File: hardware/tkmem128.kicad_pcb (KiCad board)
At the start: 2 copper layers, 78.7 x 66 mm, 24 parts, among them J1 Para a expansora, U1 GAL20V8B, U2 74HCT273, U3 AS6C1008-55PCN, U4 27C256

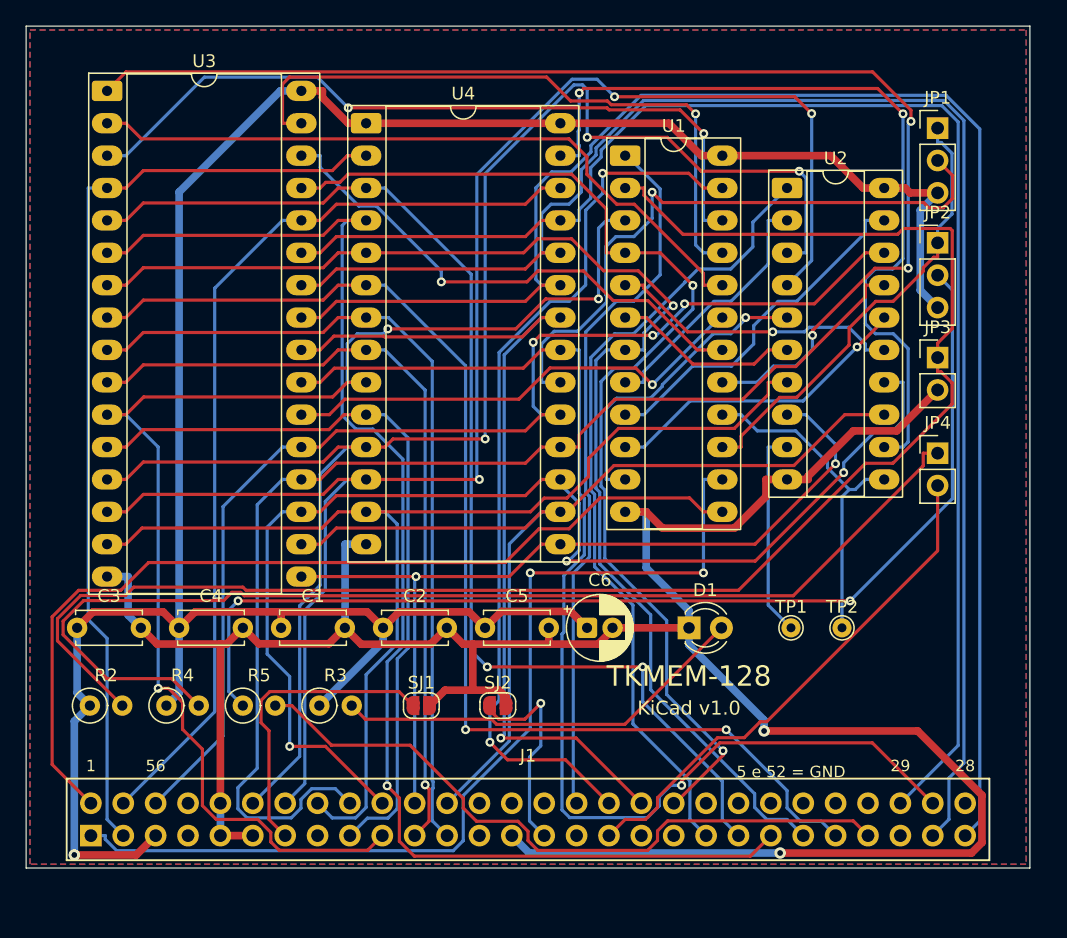
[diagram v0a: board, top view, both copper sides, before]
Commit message: Correcoes de revisao: pino 17, expansora dimensionada, .jed verificado
Correcoes apontadas na revisao:

- "Edu Luccas" -> "Eduardo Luccas" em toda a documentacao.

- O pino 17 do barramento NAO e livre no ZX Spectrum: os pinos 16, 17 e 18
  la sao Y, V e U do video componente. Corrigido na definicao do barramento
  e na documentacao, com aviso explicito de nunca fechar JP4 em Spectrum.
  Isso tambem sustenta a analise de por que a placa original avisava que o
  jumper na posicao errada danificava o micro: o pino util no TK e sinal de
  video no Spectrum, entao o jumper escolhia entre dois pinos diferentes, e
  os dois barramentos divergem justamente em pinos de alimentacao (34, 35,
  37).

- SJ1 e SJ2 sao opcionais e podem ficar abertos em qualquer maquina. O terra
  ja chega pelos pinos 6 e 14, que sao GND nas duas. Deixado explicito no
  README, na montagem e no verso da placa.

- Encaixe na caixa conferido contra os desenhos tecnicos da Patola: a tampa
  tem 81 x 69 mm internos e a placa principal (78,74 x 66,04) cabe com folga.
  Ja a expansora de 45 mm sobrava so 6,5 mm de cada lado da caixa de 32 mm -
  insuficiente para o soquete alcancar o TK. Alongada para 70 mm (19 mm de
  cada lado) e com as paredes da caixa marcadas na serigrafia.

- O .jed do GAL agora vai pronto: hardware/gal/tkmem128.jed, checksum C5752.
  Gerado por tools/galgen.py a partir das equacoes do projeto, com o mapa de
  colunas da matriz AND deduzido das proprias equacoes, e conferido fusivel a
  fusivel contra o mapa de referencia: zero divergencias em 2706 fusiveis.

Roteamento: as duas placas fecham 100% em 2 camadas com isolacao de 0,14 mm.
A ultima ligacao da placa principal exigiu um roteador de labirinto proprio
(tools/maze.py). ERC e DRC zerados; netlist reconferida no a no.

Co-Authored-By: Claude Opus 5 <noreply@anthropic.com>
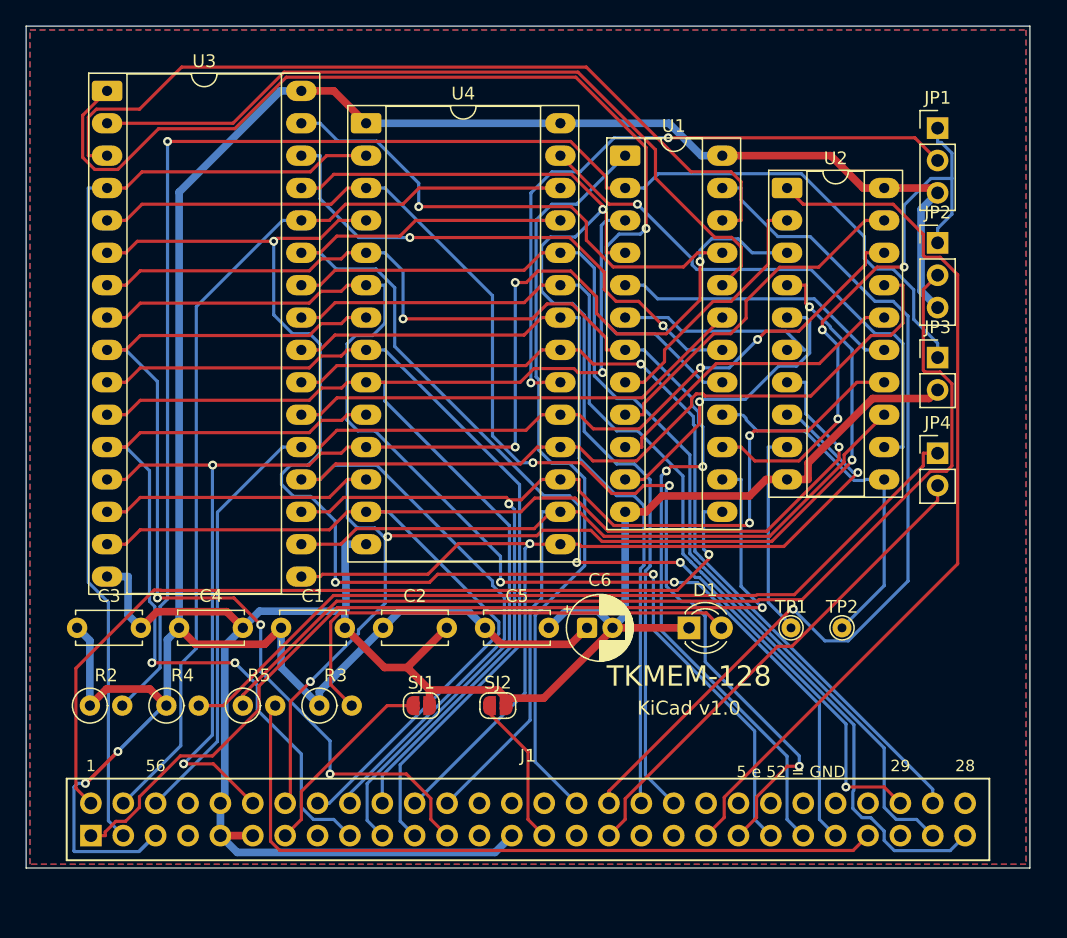
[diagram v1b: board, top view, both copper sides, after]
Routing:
- net GND: track 205.3 -> 157.9 mm, vias 2 -> 0
- net A11: track 125.8 -> 84.8 mm
- net A9: track 121.8 -> 81.7 mm
- net RAMDIS_DRV: track 88.9 -> 66.6 mm
- net A10: track 94.2 -> 72.1 mm
- net ROMA14: track 64.8 -> 42.8 mm, vias 2 -> 1
- net A8: track 114.4 -> 94.8 mm, vias 0 -> 3
- net D1: track 127.9 -> 109.8 mm, vias 3 -> 4
- net D0: track 124.9 -> 107.3 mm, vias 3 -> 5
- net D2: track 90.7 -> 105.5 mm, vias 0 -> 1
- net SA18: track 96.6 -> 83.0 mm, vias 3 -> 1
- net A3: track 65.7 -> 78.4 mm, vias 0 -> 3
- net ROMCS_N: track 35.7 -> 46.9 mm, vias 0 -> 3
- net ZX512: track 128.8 -> 117.6 mm, vias 0 -> 1
- net SA15: track 51.0 -> 40.1 mm
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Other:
- board text added: "NAO feche JP4 em ZX Spectrum: o pino 17 la e o V do video"
- board text added: "SJ1 e SJ2 sao terra extra, opcionais - podem ficar abertos"

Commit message: Esquematicos e silk rearranjados; pendencia do plano do soquete de borda
Esquematico das duas placas redesenhado a mao (havia simbolos saindo da
folha e sinais misturados) e serigrafia reorganizada. Conferido: ERC 0,
DRC 0, e a netlist exportada bate no a no com a intencao de projeto nas
duas placas (74 e 53 nets, zero divergencia).

Os geradores em tools/ passam a ser ferramenta de bootstrap: gen_schematic.py
e gen_pcb.py sobrescreveriam o ajuste manual. A fonte corrente e o conteudo
de hardware/. Documentado no README de tools/.

Registrada uma pendencia real da placa expansora (item 1b de
docs/ANTES-DE-FABRICAR.md): nas placas originais a fenda do soquete que
recebe os dedos do TK fica NO PLANO da placa, alinhada com os dedos de
passagem. O footprint atual e uma grade 2x28 de furos comuns, ou seja, o
conector monta por cima e a fenda fica alguns milimetros acima do plano —
o que joga a expansora abaixo do plano do TK e faz o periferico seguinte da
corrente descer outro tanto. Falta medir o conector para decidir entre
straddle mount e montagem por baixo.

Saidas de fabricacao e renders regerados a partir dos arquivos revisados.

Co-Authored-By: Claude Opus 5 <noreply@anthropic.com>
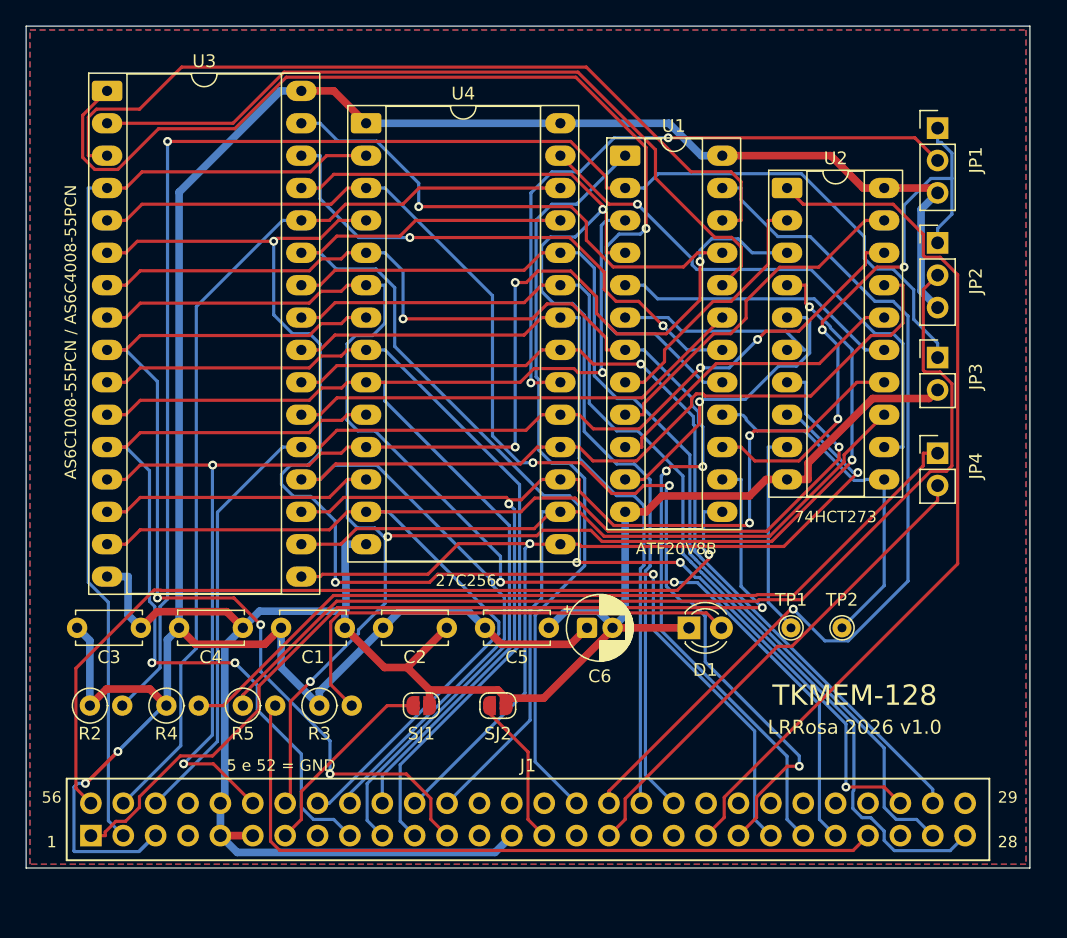
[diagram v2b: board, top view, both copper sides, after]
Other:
- board text added: "27C256"
- board text added: "74HCT273"
- board text added: "AS6C1008-55PCN / AS6C4008-55PCN"
- board text added: "ATF20V8B"
- board text added: "Derivado de Velesoft 2009 e Luccas Eletrônica 2012"
- board text added: "LRRosa 2026 v1.0"
- board text added: "NÃO feche JP4 em ZX Spectrum: o pino 17 lá é o V do vídeo"
- board text added: "SJ1 e SJ2 são terra extra, opcionais - podem ficar abertos"
- board text added: "SJ1 fechar SÓ em ZX Spectrum (pino 7 = GND lá)"
- board text added: "SJ2 fechar SÓ em TK90X/TK95 (pino 15 = GND lá)"
- board text removed: "Derivado de Velesoft 2009 e Luccas Eletronica 2012"
- board text removed: "KiCad v1.0"
- board text removed: "NAO feche JP4 em ZX Spectrum: o pino 17 la e o V do video"
- board text removed: "SJ1 e SJ2 sao terra extra, opcionais - podem ficar abertos"
- board text removed: "SJ1 fechar SO em ZX Spectrum (pino 7 = GND la)"
- board text removed: "SJ2 fechar SO em TK90X/TK95 (pino 15 = GND la)"
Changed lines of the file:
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@@
 		(tags "Through hole pin header THT 1x03 2.54mm single row")
 		(property "Reference" "JP2"
-			(at 0 -2.38 0)
+			(at 3 3 -90)
 			(layer "F.SilkS")
 			(effects
@@
 		(tags "test point THT pad")
 		(property "Reference" "TP2"
-			(at 0 -1.648 0)
+			(at 0 -2.2 0)
 			(layer "F.SilkS")
 			(effects
@@
 		(tags "Through hole pin header THT 1x03 2.54mm single row")
 		(property "Reference" "JP1"
-			(at 0 -2.38 0)
+			(at 3 2.5 -90)
 			(layer "F.SilkS")
 			(effects
@@
 		(tags "C Disc series Radial pin pitch 5.00mm diameter 5mm width 2.5mm Capacitor")
 		(property "Reference" "C5"
-			(at 2.5 -2.5 0)
+			(at 2.5 2.3 0)
 			(layer "F.SilkS")
 			(effects
@@
 		(tags "C Disc series Radial pin pitch 5.00mm diameter 5mm width 2.5mm Capacitor")
 		(property "Reference" "C4"
-			(at 2.5 -2.5 0)
+			(at 2.5 2.3 0)
 			(layer "F.SilkS")
 			(effects
@@
 		(tags "Resistor Axial_DIN0207 series Axial Vertical pin pitch 2.54mm 0.25W = 1/4W length 6.3mm diameter 2.5mm")
 		(property "Reference" "R3"
-			(at 1.27 -2.37 0)
+			(at 0 2.2 0)
 			(layer "F.SilkS")
 			(effects
@@
 		(tags "test point THT pad")
 		(property "Reference" "TP1"
-			(at 0 -1.648 0)
+			(at 0 -2.2 0)
 			(layer "F.SilkS")
 			(effects
@@
 		(tags "C Disc series Radial pin pitch 5.00mm diameter 5mm width 2.5mm Capacitor")
 		(property "Reference" "C2"
-			(at 2.5 -2.5 0)
+			(at 2.5 2.3 0)
 			(layer "F.SilkS")
 			(effects
@@
 		(tags "Through hole pin header THT 1x02 2.54mm single row")
 		(property "Reference" "JP4"
-			(at 0 -2.38 0)
+			(at 3 1 -90)
 			(layer "F.SilkS")
 			(effects
@@
 		(tags "Resistor Axial_DIN0207 series Axial Vertical pin pitch 2.54mm 0.25W = 1/4W length 6.3mm diameter 2.5mm")
 		(property "Reference" "R5"
-			(at 1.27 -2.37 0)
+			(at 0 2.2 0)
 			(layer "F.SilkS")
 			(effects
@@
 		(tags "header 2x28 TK90X TK95 interligacao placas")
 		(property "Reference" "J1"
-			(at 0 -5 0)
+			(at 0 -4.23 0)
 			(layer "F.SilkS")
 			(effects
@@
 			(layer "F.CrtYd")
 		)
-		(fp_text user "1"
-			(at -34.29 -4.2 0)
+		(fp_text user "56"
+			(at -37.37 -1.73 0)
 			(layer "F.SilkS")
 			(effects
@@
 			)
 		)
-		(fp_text user "56"
-			(at -29.21 -4.2 0)
+		(fp_text user "1"
+			(at -37.37 1.77 0)
 			(layer "F.SilkS")
 			(effects
@@
 		)
 		(fp_text user "29"
-			(at 29.21 -4.2 0)
+			(at 37.63 -1.73 0)
 			(layer "F.SilkS")
 			(effects
@@
 		)
 		(fp_text user "28"
-			(at 34.29 -4.2 0)
+			(at 37.63 1.77 0)
 			(layer "F.SilkS")
 			(effects
@@
 		(tags "CP Radial series Radial pin pitch 2.00mm diameter 5mm height 7mm Electrolytic Capacitor")
 		(property "Reference" "C6"
-			(at 1 -3.75 0)
+			(at 1 3.8 0)
 			(layer "F.SilkS")
 			(effects
@@
 		(tags "LED")
 		(property "Reference" "D1"
-			(at 1.27 -2.96 0)
+			(at 1.27 3.3 0)
 			(layer "F.SilkS")
 			(effects
@@
 		(tags "solder jumper open")
 		(property "Reference" "SJ1"
-			(at 0 -1.8 0)
+			(at 0 2.2 0)
 			(layer "F.SilkS")
 			(effects
@@
 		(tags "C Disc series Radial pin pitch 5.00mm diameter 5mm width 2.5mm Capacitor")
 		(property "Reference" "C1"
-			(at 2.5 -2.5 0)
+			(at 2.5 2.3 0)
 			(layer "F.SilkS")
 			(effects
@@
 		(tags "C Disc series Radial pin pitch 5.00mm diameter 5mm width 2.5mm Capacitor")
 		(property "Reference" "C3"
-			(at 2.5 -2.5 0)
+			(at 2.5 2.3 0)
 			(layer "F.SilkS")
 			(effects
@@
 		(tags "Resistor Axial_DIN0207 series Axial Vertical pin pitch 2.54mm 0.25W = 1/4W length 6.3mm diameter 2.5mm")
 		(property "Reference" "R4"
-			(at 1.27 -2.37 0)
+			(at 0 2.2 0)
 			(layer "F.SilkS")
 			(effects
@@
 		(tags "solder jumper open")
 		(property "Reference" "SJ2"
-			(at 0 -1.8 0)
+			(at 0 2.2 0)
 			(layer "F.SilkS")
 			(effects
@@
 		(tags "Resistor Axial_DIN0207 series Axial Vertical pin pitch 2.54mm 0.25W = 1/4W length 6.3mm diameter 2.5mm")
 		(property "Reference" "R2"
-			(at 1.27 -2.37 0)
+			(at 0 2.2 0)
 			(layer "F.SilkS")
 			(effects
@@
 		(tags "Through hole pin header THT 1x02 2.54mm single row")
 		(property "Reference" "JP3"
-			(at 0 -2.38 0)
+			(at 3 1.5 -90)
 			(layer "F.SilkS")
 			(effects
@@
 	)
 	(gr_text "5 e 52 = GND"
-		(at 60 58.5 0)
+		(at 20 58 0)
+		(layer "F.SilkS")
+		(effects
+			(font
+				(size 0.9 0.9)
+				(thickness 0.15)
+			)
+		)
+	)
+	(gr_text "27C256"
+		(at 34.5 43.5 0)
+		(layer "F.SilkS")
+		(effects
+			(font
+				(size 0.9 0.9)
+				(thickness 0.15)
+			)
+		)
+	)
+	(gr_text "ATF20V8B"
+		(at 51 41 0)
 		(layer "F.SilkS")
 		(effects
@@
 		)
 	)
-	(gr_text "KiCad v1.0"
-		(at 52 53.5 0)
+	(gr_text "74HCT273"
+		(at 63.5 38.5 0)
+		(layer "F.SilkS")
+		(effects
+			(font
+				(size 0.9 0.9)
+				(thickness 0.15)
+			)
+		)
+	)
+	(gr_text "AS6C1008-55PCN / AS6C4008-55PCN"
+		(at 3.5 24 90)
+		(layer "F.SilkS")
+		(effects
+			(font
+				(size 0.9 0.9)
+				(thickness 0.15)
+			)
+		)
+	)
+	(gr_text "LRRosa 2026 v1.0"
+		(at 65 55 0)
 		(layer "F.SilkS")
 		(effects
@@
 	)
 	(gr_text "TKMEM-128"
-		(at 52 51 0)
+		(at 65 52.5 0)
 		(layer "F.SilkS")
 		(effects
@@
 		)
 	)
-	(gr_text "     NAO feche JP4 em ZX Spectrum: o pino 17 la e o V do video"
-		(at 39.37 19.5 0)
+	(gr_text "     NÃO feche JP4 em ZX Spectrum: o pino 17 lá é o V do vídeo"
+		(at 30.5 26 -90)
 		(layer "B.SilkS")
 		(effects
@@
 		)
 	)
-	(gr_text "SJ1 e SJ2 sao terra extra, opcionais - podem ficar abertos"
-		(at 39.37 22.5 0)
+	(gr_text "SJ2  fechar SÓ em TK90X/TK95 (pino 15 = GND lá)"
+		(at 11 26.2 -90)
 		(layer "B.SilkS")
 		(effects
@@
 		)
 	)
-	(gr_text "SJ1  fechar SO em ZX Spectrum (pino 7 = GND la)"
-		(at 39.37 25 0)
+	(gr_text "SJ1  fechar SÓ em ZX Spectrum (pino 7 = GND lá)"
+		(at 13.5 26.5 -90)
 		(layer "B.SilkS")
 		(effects
@@
 		)
 	)
-	(gr_text "SJ2  fechar SO em TK90X/TK95 (pino 15 = GND la)"
-		(at 39.37 27.5 0)
+	(gr_text "SJ1 e SJ2 são terra extra, opcionais - podem ficar abertos"
+		(at 16 23.5 -90)
 		(layer "B.SilkS")
 		(effects
@@
 		)
 	)
-	(gr_text "Derivado de Velesoft 2009 e Luccas Eletronica 2012"
-		(at 39.37 38 0)
+	(gr_text "Derivado de Velesoft 2009 e Luccas Eletrônica 2012"
+		(at 39.5 58 0)
 		(layer "B.SilkS")
 		(effects
@@
 		)
 	)
-	(gr_text "JP1  1-2 = ROM 128   |   2-3 = ROM do TK"
-		(at 39.37 8 0)
+	(gr_text "JP4  fechado = auto-desativa a RAM de 32K do TK"
+		(at 33 24.5 -90)
 		(layer "B.SilkS")
 		(effects
@@
 		)
 	)
-	(gr_text "JP2  aberto = ROM do TK  |  1-2 = pelo GAL  |  2-3 = +5V"
-		(at 39.37 11 0)
+	(gr_text "JP3  fechado = 512K (AS6C4008)"
+		(at 38 31.7037 -90)
 		(layer "B.SilkS")
 		(effects
@@
 		)
 	)
-	(gr_text "JP3  fechado = 512K (AS6C4008)"
-		(at 39.37 14 0)
+	(gr_text "JP2  aberto = ROM do TK  |  1-2 = pelo GAL  |  2-3 = +5V"
+		(at 62.5 28.5 -90)
 		(layer "B.SilkS")
 		(effects
@@
 		)
 	)
-	(gr_text "JP4  fechado = auto-desativa a RAM de 32K do TK"
-		(at 39.37 17 0)
+	(gr_text "JP1  1-2 = ROM 128   |   2-3 = ROM do TK"
+		(at 65 35 -90)
 		(layer "B.SilkS")
 		(effects
@@
 	)
 	(gr_text "github.com/lrrosa/tkmem128-kicad"
-		(at 39.37 35 0)
+		(at 39.5 55 0)
 		(layer "B.SilkS")
 		(effects
@@
 	)
 	(gr_text "CERN-OHL-S v2"
-		(at 39.37 32 0)
+		(at 39.5 52 0)
 		(layer "B.SilkS")
 		(effects
